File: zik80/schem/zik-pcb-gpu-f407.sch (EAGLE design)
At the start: 48 parts

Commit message: GPU rev2 designed, ready to send up to elecrow .. *fear*
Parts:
- removed D3, D4, D5, D6: 1N5400, diode:1N5400
- removed JP1, JP2, JP3, JP4: (no value), pinhead:PINHD-1X16
- removed JP6, JP7, JP8, JP9: (no value), pinhead:PINHD-1X3
- removed U$1: STM32F405R, stm32f4:STM32F405R
- added +3V3OUT, +5OUT, GNDOUT: (no value), pinhead:PINHD-1X3
- added 1-25, 26-50, 51-75, 76-100: (no value), pinhead:PINHD-2X13
- added ADDRESS_BUS: (no value), pinhead:PINHD-2X11
- added C11, C12: .1uF, rcl:C-EU025-025X050
- added CTRL_BUS: (no value), pinhead:PINHD-2X8
- added D10, D7, D8, D9: 1N4004, diode:1N4004
- added DATA_BUS: (no value), pinhead:PINHD-1X8
- added STM32F4: STM32F407V, stm32f4:STM32F407V
- D1, D2: value 1N5400 -> 1N4004; device diode:1N5400 -> diode:1N4004
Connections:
- removed net N$10: GPUHDR.6
- new net PD0: 76-100.6, DATA_BUS.1, STM32F4.PD0/CAN1_RX(5T)
- new net PD1: 76-100.7, DATA_BUS.2, STM32F4.PD1/CAN1_TX(5T)
- new net PD10: 51-75.7, ADDRESS_BUS.19, STM32F4.PD10(5T)
- new net PD11: 51-75.8, ADDRESS_BUS.20, STM32F4.PD11(5T)
- new net PD12: 51-75.9, ADDRESS_BUS.21, STM32F4.PD12/TIM4_CH1(5T)
- new net PD13: 51-75.10, ADDRESS_BUS.22, STM32F4.PD13/TIM4_CH2(5T)
- new net PD14: 51-75.11, STM32F4.PD14/TIM4_CH3(5T)
- new net PD15: 51-75.12, STM32F4.PD15/TIM4_CH4(5T)
- new net PD3: 76-100.9, DATA_BUS.4, STM32F4.PD3(5T)
- new net PD4: 76-100.10, DATA_BUS.5, STM32F4.PD4(5T)
- new net PD5: 76-100.11, DATA_BUS.6, STM32F4.PD5/USART2_TX(5T)
- new net PD6: 76-100.12, DATA_BUS.7, STM32F4.PD6/USART2_RX(5T)
- new net PD7: 76-100.13, DATA_BUS.8, STM32F4.PD7(5T)
- new net PD8: 51-75.5, ADDRESS_BUS.17, STM32F4.PD8/USART3_TX(5T)
- new net PD9: 51-75.6, ADDRESS_BUS.18, STM32F4.PD9/USART3_RX(5T)
- new net PE0: 76-100.22, ADDRESS_BUS.1, STM32F4.PE0(5T)
- new net PE1: 76-100.23, ADDRESS_BUS.2, STM32F4.PE1(5T)
- new net PE10: 26-50.16, ADDRESS_BUS.11, STM32F4.PE10/TIM1_CH2N(5T)
- new net PE11: 26-50.17, ADDRESS_BUS.12, STM32F4.PE11/TIM1_CH2(5T)
- new net PE12: 26-50.18, ADDRESS_BUS.13, STM32F4.PE12/TIM1_CH3N(5T)
- new net PE13: 26-50.19, ADDRESS_BUS.14, STM32F4.PE13/TIM1_CH3(5T)
- new net PE14: 26-50.20, ADDRESS_BUS.15, STM32F4.PE14/TIM1_CH4(5T)
- new net PE15: 26-50.21, ADDRESS_BUS.16, STM32F4.PE15/TIM1_BKIN(5T)
- new net PE2: 1-25.1, ADDRESS_BUS.3, STM32F4.PE2/ETH_MII_TXD3(5T)
- new net PE3: 1-25.2, ADDRESS_BUS.4, STM32F4.PE3(5T)
- new net PE4: 1-25.3, ADDRESS_BUS.5, STM32F4.PE4(5T)
- new net PE5: 1-25.4, ADDRESS_BUS.6, STM32F4.PE5/TIM9_CH1(5T)
- new net PE6: 1-25.5, ADDRESS_BUS.7, STM32F4.PE6/TIM9_CH2(5T)
- new net PE7: 26-50.13, ADDRESS_BUS.8, STM32F4.PE7/TIM1_ETR(5T)
- new net PE8: 26-50.14, ADDRESS_BUS.9, STM32F4.PE8/TIM1_CH1N(5T)
- new net PE9: 26-50.15, ADDRESS_BUS.10, STM32F4.PE9/TIM1_CH1(5T)
- net +3V3: now also +3V3OUT.1, +3V3OUT.2, +3V3OUT.3, 1-25.11, 1-25.19, 1-25.21, 1-25.22, 26-50.25, 26-50.3, 51-75.25, 76-100.25, C11.1, C12.1, STM32F4.VDDA, STM32F4.VDD_1, STM32F4.VDD_2, STM32F4.VDD_3, STM32F4.VDD_4, STM32F4.VDD_5, STM32F4.VDD_6, STM32F4.VREF+; no longer JP1.13, JP2.16, JP2.3, JP3.16, JP4.16, JP7.1, JP7.2, JP7.3, U$1.VDDA, U$1.VDD_1, U$1.VDD_2, U$1.VDD_3, U$1.VDD_4
- net +5V: now also +5OUT.1, +5OUT.2, +5OUT.3; no longer JP6.1, JP6.2, JP6.3
- net BOOT0: now also 76-100.19, STM32F4.BOOT0; no longer JP4.12, U$1.BOOT0
- net GND: now also 1-25.10, 1-25.20, 26-50.2, 51-75.24, 76-100.24, C11.2, C12.2, GNDOUT.1, GNDOUT.2, GNDOUT.3, STM32F4.VSSA, STM32F4.VSS_1, STM32F4.VSS_2, STM32F4.VSS_3, STM32F4.VSS_4; no longer JP1.12, JP2.2, JP4.15, JP8.1, JP8.2, JP8.3, U$1.VSSA, U$1.VSS_1, U$1.VSS_2
- net N$12: now also D9.C; no longer D3.C
- net N$14: now also D10.C; no longer D4.C
- net N$17: now also D1.C; no longer D5.C
- net N$19: now also D2.C; no longer D6.C
- net N$4: now also D7.C; no longer D1.C
- net N$7: now also D8.C; no longer D2.C
- net NRST: now also 1-25.14, ISPJTAG.15, STM32F4.NRST; no longer JP1.7, U$1.NRST
- net PA0: now also 1-25.23, STM32F4.PA0/ETH_MII_CRS/ADC123_IN0(5T); no longer JP1.14, U$1.PA0/ADC123_IN0(5T)
- net PA1: now also 1-25.24, STM32F4.PA1/ETH_RMII_RX_CLK/ADC123_IN1(5T); no longer JP1.15, U$1.PA1/ADC123_IN1(5T)
- net PA10: now also 51-75.19, STM32F4.PA10/USART1_RX(5T); no longer JP3.11, U$1.PA10/TIM1_CH3/USART1_RX(5T)
- net PA11: now also 51-75.20, STM32F4.PA11/USART1_CTS(5T); no longer JP3.12, U$1.PA11/TIM1_CH4/CANRX/USBDM(5T)
- net PA12: now also 51-75.21, STM32F4.PA12/USART1_RTS(5T); no longer JP3.13, U$1.PA12/CANTX/USBDP(5T)
- net PA13: now also 51-75.22, STM32F4.PA13/JTMS-SWDAT(5T); no longer JP3.14, U$1.PA13/JTMS-SWDAT(5T)
- net PA14: now also 76-100.1, STM32F4.PA14/JTCK-SWCLK(5T); no longer JP4.1, U$1.PA14/JTCK-SWCLK(5T)
- net PA15: now also 76-100.2, STM32F4.PA15/JTDI(5T); no longer JP4.2, U$1.PA15/JTDI(5T)
- net PA2: now also 1-25.25, STM32F4.PA2/ETH_MDIO/ADC123_IN2(5T); no longer JP1.16, U$1.PA2/ADC123_IN2(5T)
- net PA3: now also 26-50.1, STM32F4.PA3/ETH_MII_COL/ADC123_IN2(5T); no longer JP2.1, U$1.PA3/ADC123_IN3(5T)
- net PA4: now also 26-50.4, STM32F4.PA4/ADC12_IN4; no longer JP2.4, U$1.PA4/ADC12_IN4
- net PA5: now also 26-50.5, STM32F4.PA5/SPI1_SCK/ADC12_IN5; no longer JP2.5, U$1.PA5/ADC12_IN5
- net PA6: now also 26-50.6, STM32F4.PA6/SPI1_MISO/ADC12_IN6(5T); no longer JP2.6, U$1.PA6/ADC12_IN6(5T)
- net PA7: now also 26-50.7, STM32F4.PA7/ETH_MII_RX_DV/ADC12_IN7(5T); no longer JP2.7, U$1.PA7/TIM1_CH1N/ADC12_IN7(FT)
- net PA8: now also 51-75.17, STM32F4.PA8/MCO1(5T); no longer JP3.9, U$1.PA8/TIM1_CH1(5T)
- net PA9: now also 51-75.18, STM32F4.PA9/USART1_TX(5T); no longer JP3.10, U$1.PA9/TIM1_CH2/USART1_TX(5T)
- net PB0: now also 26-50.10, CTRL_BUS.1, CTRL_BUS.2, STM32F4.PB0/ETH_MII_RXD2/ADC12_IN8(5T); no longer JP2.10, U$1.PB0/TIM1_CH2N/ADC12_IN8(5T)
- net PB1: now also 26-50.11, CTRL_BUS.3, CTRL_BUS.4, STM32F4.PB1/ETH_MII_RXD3/ADC12_IN9(5T); no longer JP2.11, U$1.PB1/TIM1_CH3N/ADC12_IN9(5T)
- net PB10: now also 26-50.22, STM32F4.PB10/ETH_MII_RX_ER(5T); no longer JP2.13, U$1.PB10/I2C2_SCL(5T)
- net PB11: now also 26-50.23, STM32F4.PB11/ETH_MII_TX_EN(5T); no longer JP2.14, U$1.PB11/I2C2_SDA(5T)
- net PB12: now also 51-75.1, STM32F4.PB12/ETH_MII_TXD0(5T); no longer JP3.1, U$1.PB12(5T)
- net PB13: now also 51-75.2, STM32F4.PB13/ETH_MII_TXD1(5T); no longer JP3.2, U$1.PB13/SPI2_SCK(5T)
- net PB14: now also 51-75.3, STM32F4.PB14/TIM8_CH2N(5T); no longer JP3.3, U$1.PB14/SPI2_MISO(5T)
- net PB15: now also 51-75.4, STM32F4.PB15/TIM8_CH3N(5T); no longer JP3.4, U$1.PB15/SPI2_MOSI(5T)
- net PB2: now also 26-50.12, CTRL_BUS.5, CTRL_BUS.6, STM32F4.PB2/BOOT1(5T); no longer JP2.12, U$1.PB2/BOOT1(5T)
- net PB3: now also 76-100.14, CTRL_BUS.7, CTRL_BUS.8, STM32F4.PB3/JTDO(5T); no longer JP4.7, U$1.PB3/JTDO(5T)
- net PB4: now also 76-100.15, CTRL_BUS.10, CTRL_BUS.9, STM32F4.PB4/JNTRST(5T); no longer ISPJTAG.15, JP4.8, U$1.PB4/JNTRST(5T)
- net PB5: now also 76-100.16, CTRL_BUS.11, CTRL_BUS.12, STM32F4.PB5/TIM3_CH2(5T); no longer JP4.9, U$1.PB5(5T)
- net PB6: now also 76-100.17, STM32F4.PB6/I2C1_SCL(5T); no longer JP4.10, U$1.PB6/I2C1_SCL/USART1_TX/TIM4_CH1(5T)
- net PB7: now also 76-100.18, STM32F4.PB7/I2C1_SDA(5T); no longer JP4.11, U$1.PB7/I2C1_SDA/USART1_RX/TIM4_CH2(5T)
- net PB8: now also 76-100.20, CTRL_BUS.13, CTRL_BUS.14, STM32F4.PB8/TIM10_CH1(5T); no longer JP4.13, U$1.PB8/TIM10_CH1/TIM4_CH3(5T)
- net PB9: now also 76-100.21, CTRL_BUS.15, CTRL_BUS.16, STM32F4.PB9/TIM11_CH1(5T); no longer JP4.14, U$1.PB9/TIM11_CH1/TIM4_CH4(5T)
- net PC0: now also 1-25.15, STM32F4.PC0/ADC123_IN10(5T); no longer JP1.8, U$1.PC0/ADC123_IN10(5T)
- net PC1: now also 1-25.16, STM32F4.PC1/ETH_MDC/ADC123_IN11(5T); no longer JP1.9, U$1.PC1/ADC123_IN11(5T)
- net PC10: now also 76-100.3, STM32F4.PC10/UART4_TX(5T); no longer JP4.3, U$1.PC10(5T)
- net PC11: now also 76-100.4, STM32F4.PC11/UART4_RX(5T); no longer JP4.4, U$1.PC11(5T)
- net PC12: now also 76-100.5, STM32F4.PC12/UART5_TX(5T); no longer JP4.5, U$1.PC12(5T)
- net PC13: now also 1-25.7, STM32F4.PC13(5T); no longer JP1.2, U$1.PC13(5T)
- net PC14: now also 1-25.8, STM32F4.PC14/OSC32_IN(5T); no longer JP1.3, U$1.PC14/OSC32_IN(5T)
- net PC15: now also 1-25.9, STM32F4.PC15/OSC32_OUT(5T); no longer JP1.4, U$1.PC15/OSC32_OUT(5T)
- net PC2: now also 1-25.17, STM32F4.PC2/ETH_MII_TXD2/ADC123_IN12(5T); no longer JP1.10, U$1.PC2/ADC123_IN12(5T)
- net PC3: now also 1-25.18, STM32F4.PC3/ETH_MII_TX_CLK/ADC123_IN13(5T); no longer JP1.11, U$1.PC3/ADC123_IN13(5T)
- net PC4: now also 26-50.8, STM32F4.PC4/ETH_MII_RXD0/ADC12_IN14(5T); no longer JP2.8, U$1.PC4/ADC12_IN14
- net PC5: now also 26-50.9, STM32F4.PC5/ETH_MII_RXD1/ADC12_IN15(5T); no longer JP2.9, U$1.PC5/ADC12_IN15
- net PC6: now also 51-75.13, D7.A, D9.A, STM32F4.PC6/TIM3_CH1(5T); no longer D3.A, D5.A, JP3.5, U$1.PC6/TIM3_CH1/TIM_CH1/USART6_TX(5T)
- net PC7: now also 51-75.14, D10.A, D8.A, STM32F4.PC7/TIM8_CH2(5T); no longer D4.A, D6.A, JP3.6, U$1.PC7/TIM3_CH2/TIM8_CH2/USART6_RX(5T)
- net PC8: now also 51-75.15, STM32F4.PC8/TIM8_CH3(5T); no longer JP3.7, U$1.PC8/TIM3_CH3/TIM8_CH3(5T)
- net PC9: now also 51-75.16, STM32F4.PC9/TIM3_CH4(5T); no longer JP3.8, U$1.PC9/TIM3_CH4/TIM8_CH4(5T)
- net PD2: now also 76-100.8, DATA_BUS.3, STM32F4.PD2/UART5_RX(5T); no longer JP4.6, U$1.PD2/TIM3_ETR(5T)
- net PH0: now also 1-25.12, STM32F4.PH0-OSC_IN(5T); no longer JP1.5, U$1.PH0/OSC_IN(5T)
- net PH1: now also 1-25.13, STM32F4.PH1-OSC_OUT(5T); no longer JP1.6, U$1.PH1/OSC_OUT(5T)
- net VBAT: now also 1-25.6, STM32F4.VBAT; no longer JP1.1, U$1.VBAT
- net VCAP_1: now also 26-50.24, STM32F4.VCAP1; no longer JP2.15, U$1.VCAP_1
- net VCAP_2: now also 51-75.23, STM32F4.VCAP2; no longer JP3.15, U$1.VCAP_2
- net VCC: no longer JP9.1, JP9.2, JP9.3
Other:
- note added: "/OE /WE n/c n/c n/c n/c /BUSREQ /BUSACK"
- note added: "Double-header - in case we need to add signals from BoB headers, or ..etc Longer header - in case needed for ROM control somehow.. etc"
- note added: "PA2-3 == serial console PA8-PA12 = serial control in/out PB0-5 = ctrl bus OE WE n/c*4 PB6/PB7 = i2c sda/scl ? PB8 -> ctrl bus BUSREQ PB9 -> ctrl bus BUSACK PB10/11 == sync PB12 -> vblank PC0-5 == RGB PC6-7 = brightness PE - addr bus PD 8..13 .. addr bus PD 0..7 data bus"
- note added: "TBD Idea: - send vblank to PB2 (not used now, but wired to control bus) - accept 'frame ready' on PB3 (not used now, but wired to control bus) from cpu/base"
- note added: "TBD v2: - sync may need 80/100 resistor on some monitor - add parallel caps to decoupling caps on stm32, so can have both a electrolytic + a tant on each, without sticking both through solder point? - extra GND plane via's? - cmp pinout to datasheet"
- note removed: "BUG in r1: JTAG reset is not working; have to hit manual reset so flashing and post-flash can work right"
- note removed: "PA2-3 == serial console PA8-PA12 = serial control in/out PB6/PB7 = i2c sda/scl ? conflict USART1? PB8 -> __? grab addr/data bus? PB9 -> __? heartbeat? PB10/11 == sync PB12 -> vblank PC0-5 == RGB PC6-7 = brightness __ = flags (hsync, vsync, heartbeat..) __ = address / data / control"
- note removed: "TBD v2: - sync may need 80/100 resistor on some monitor - address/data/signal RAM bus - add parallel caps to decoupling caps on stm32, so can have both a electrolytic + a tant on each, without sticking both through solder point? - extra GND plane via's!"
- moved on the sheet: C1, C2, C3, C4, C5, C6, C7, C8, C9, D1, D2, GPUHDR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

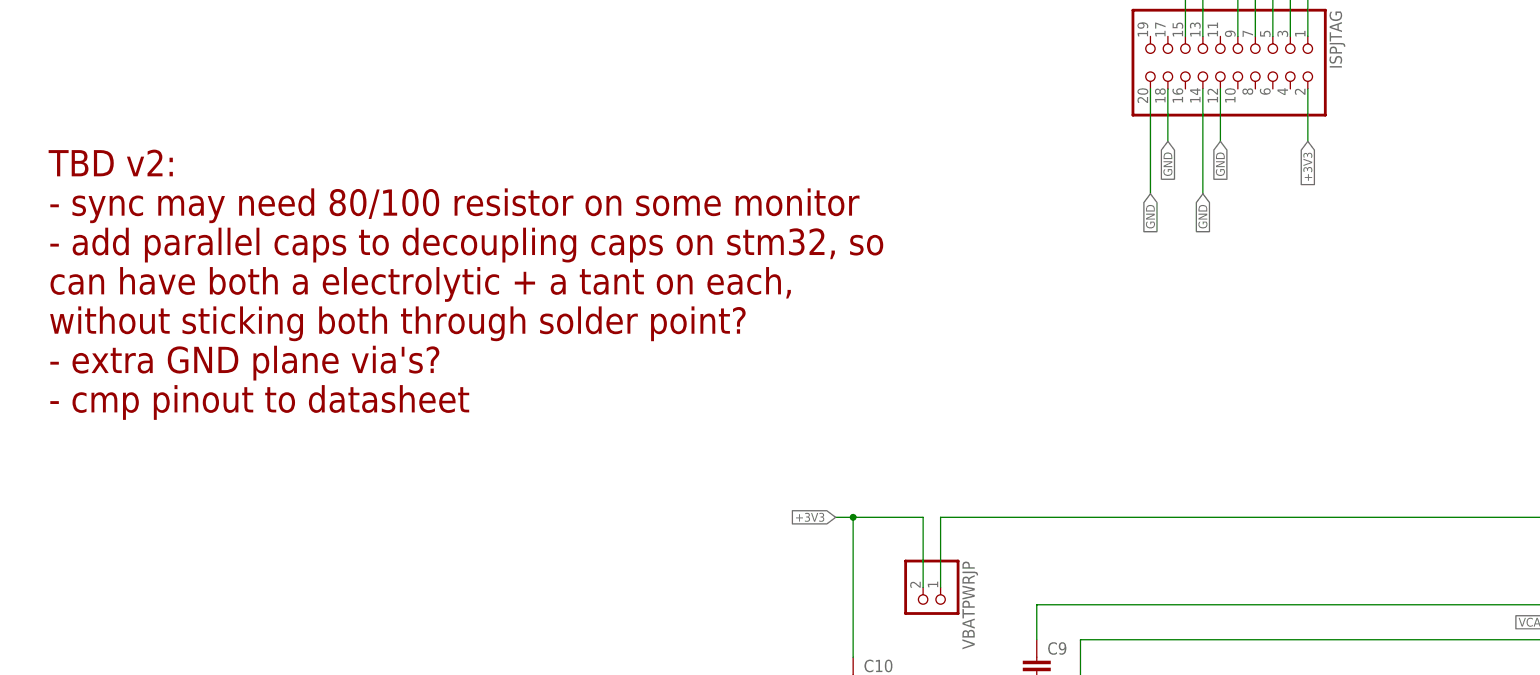
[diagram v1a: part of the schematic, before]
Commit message: Fiddling with hooking up the gpu and cpu buses .. need more IDC connector!
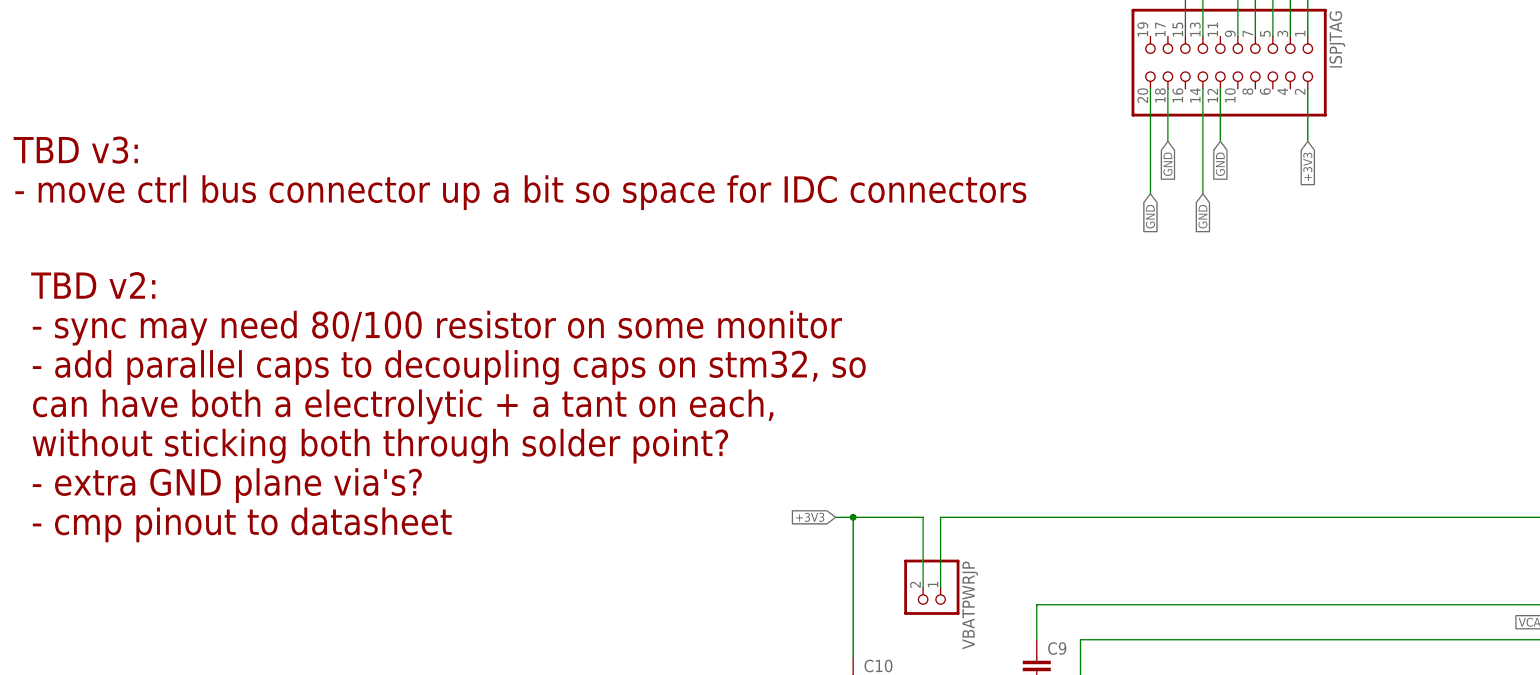
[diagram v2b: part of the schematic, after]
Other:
- note added: "TBD v3: - move ctrl bus connector up a bit so space for IDC connectors"
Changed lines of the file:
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@@
 <?xml version="1.0" encoding="utf-8"?>
 <!DOCTYPE eagle SYSTEM "eagle.dtd">
-<eagle version="6.4">
+<eagle version="6.5.0">
 <drawing>
 <settings>
@@
 - GND</text>
 <text x="-27.94" y="33.02" size="1.778" layer="94" rot="R90">2.2uF = 22pF</text>
-<text x="-168.91" y="86.36" size="3.81" layer="94">TBD v2:
+<text x="-171.45" y="68.58" size="3.81" layer="94">TBD v2:
 - sync may need 80/100 resistor on some monitor
 - add parallel caps to decoupling caps on stm32, so
@@
 but wired to control
 bus) from cpu/base</text>
+<text x="-173.99" y="116.84" size="3.81" layer="94">TBD v3:
+- move ctrl bus connector up a bit so space for IDC connectors</text>
 </plain>
 <instances>

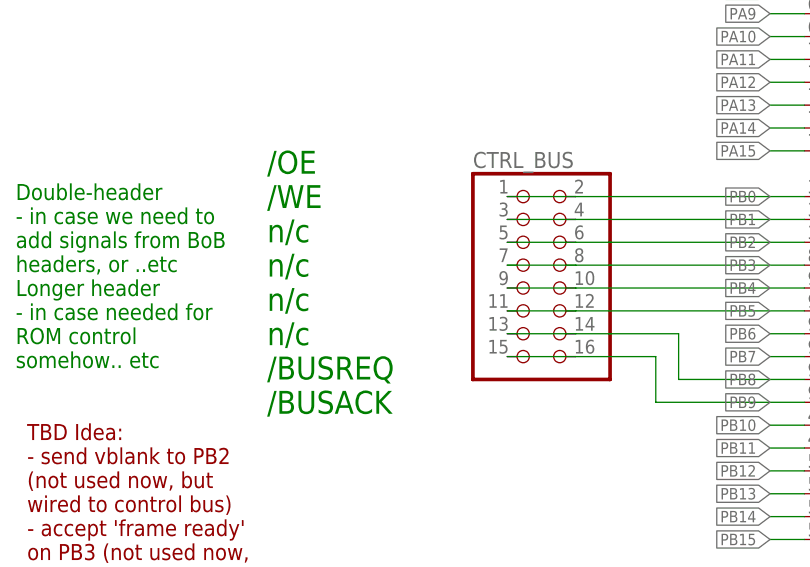
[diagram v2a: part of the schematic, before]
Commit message: Full success! eZ80 -> RAM -> GPU
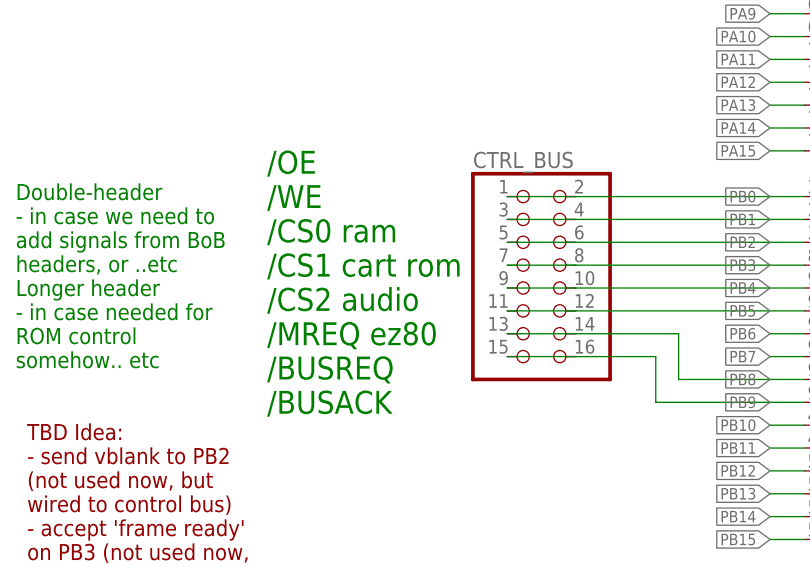
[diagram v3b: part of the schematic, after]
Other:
- note added: "/OE /WE /CS0 ram /CS1 cart rom /CS2 audio /MREQ ez80 /BUSREQ /BUSACK"
- note removed: "/OE /WE n/c n/c n/c n/c /BUSREQ /BUSACK"
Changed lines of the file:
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@@
 <text x="19.05" y="-69.85" size="2.54" layer="91">/OE
 /WE
-n/c
-n/c
-n/c
-n/c
+/CS0 ram
+/CS1 cart rom
+/CS2 audio
+/MREQ ez80
 /BUSREQ
 /BUSACK</text>
